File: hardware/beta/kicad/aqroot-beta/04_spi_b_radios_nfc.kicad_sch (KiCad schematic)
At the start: 11 parts, among them U7 E07-400M10S, U8 E22-900M22S, U9 ST25R3916_NFC_PLACEHOLDER

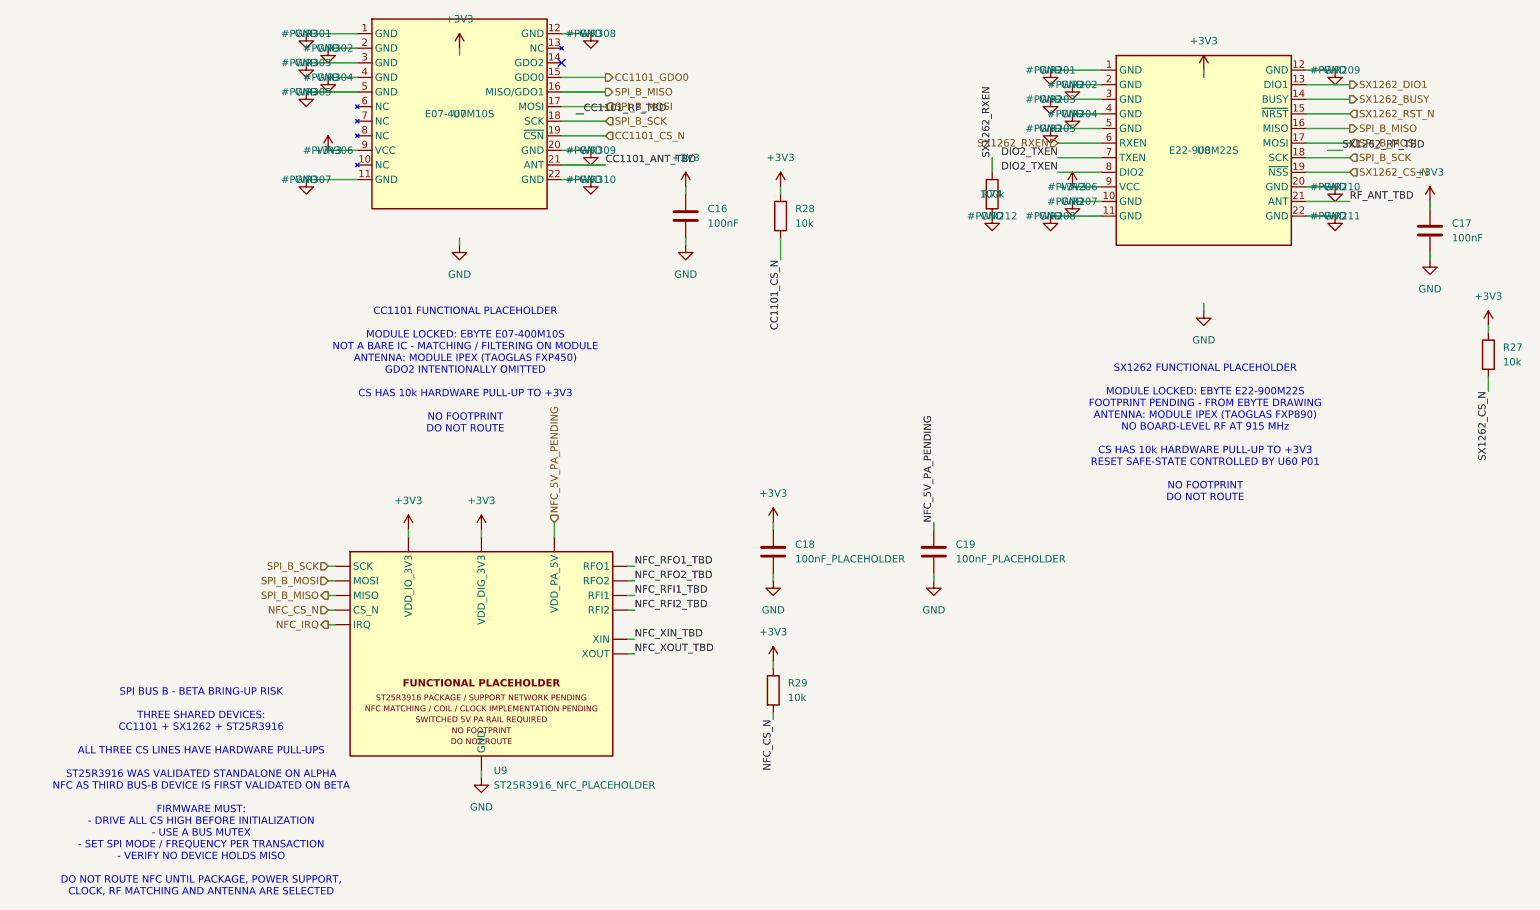
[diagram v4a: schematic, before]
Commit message: AQROOT Beta: integrate physical ST25R3916 NFC controller
Replaces the 15-pin ST25R3916_NFC_PLACEHOLDER at U9 with the physical 33-pad
ST25R3916-AQET on AQROOT_Beta:ST25R3916_AQET, and adds the ten ST-specified
decoupling capacitors. Single sheet touched, 04_spi_b_radios_nfc, plus two pin
electrical types corrected in the library.

ALL 33 PADS VERIFIED AGAINST AN EXPECTED MAP, not merely counted: the netlist was
compared pin-by-pin to the locked mapping and returned 33 of 33 with zero
mismatches. Supplies are VDD_IO on +3V3, VDD and VDD_TX both on
NFC_5V_PA_PENDING, and I2C_EN grounded to select SPI. SPI is BSS on pin 29 to
NFC_CS_N, SCLK/MOSI/MISO to SPI bus B, IRQ on pin 27 to NFC_IRQ. Grounds are
GND_D, both GND_DR, VSS, GND_A and the exposed pad 33.

THE KEY RELATIONSHIP IS CORRECT IN THE NETLIST: NFC_VDD_RF holds U9 pin 9,
U9 pin 14, C49 and C50 - the VDD_RF regulator output feeding VDD_DR with its
decoupling, which is the normal internal-regulator configuration. There is no
VDD_DR to VDD_TX and no VDD_RF to VDD_TX connection anywhere; the bypass mode is
not implemented.

TEN CAPACITORS ADDED, C45 to C54, values exactly as ST specifies and not
substituted: VDD_D 2.2uF with 10nF, VDD_A 2.2uF with 10nF, VDD_RF 2.2uF with
10nF, VDD_AM 2.2uF with 1nF, and AGDC 1uF with 10nF. The 2.2uF parts are 16V X7R
in 0805 rather than 0603 so effective capacitance survives bias, the small values
are 50V X7R 0603, and the 1uF is 16V X7R 0603. Each carries a note that it is
local decoupling requiring close placement during layout.

TWO ERC ERRORS WERE FIXED BY CORRECTING THE MODEL RATHER THAN BY ADDING
EXCLUSIONS. VDD_RF was typed as a plain output, so the power input VDD_DR it
feeds reported power_pin_not_driven; VDD_RF is genuinely a regulated supply
output and is now typed power_out, which removes the error legitimately. RFI1,
RFI2 and XTI were typed as inputs and reported pin_not_driven on their deferred
analog nets; they are analog pins into networks that do not yet exist, an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
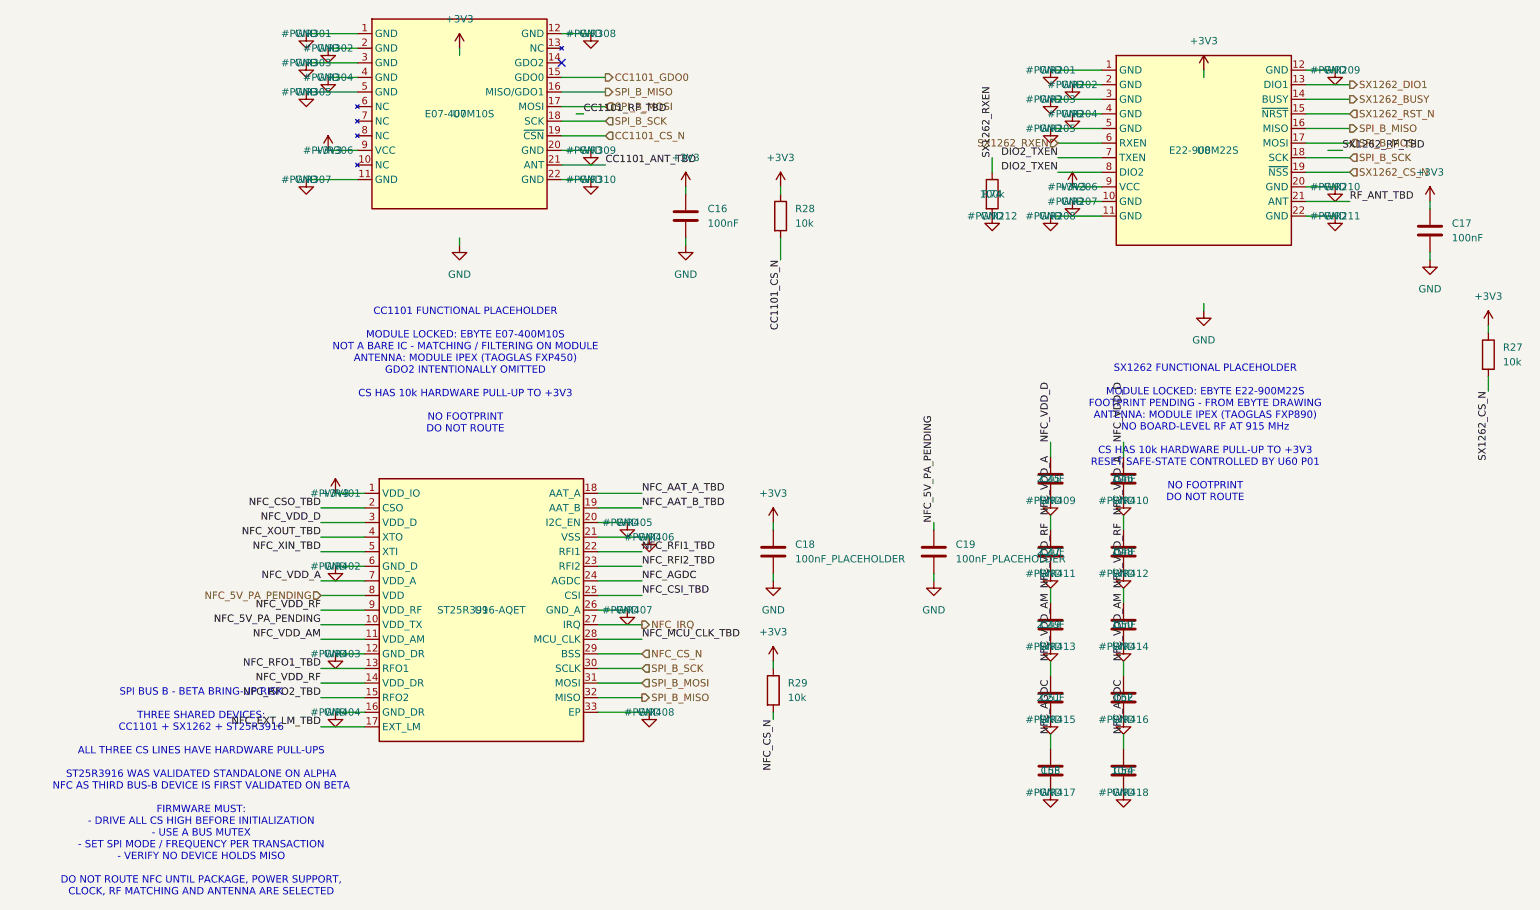
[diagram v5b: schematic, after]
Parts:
- removed U9: ST25R3916_NFC_PLACEHOLDER, symbol AQROOT_Beta:ST25R3916_NFC_PLACEHOLDER
- added C45, C47, C49, C51: 2.2uF, Capacitor_SMD:C_0805_2012Metric, symbol Device:C
- added C46, C48, C50, C54: 10nF, Capacitor_SMD:C_0603_1608Metric, symbol Device:C
- added C52: 1nF, Capacitor_SMD:C_0603_1608Metric, symbol Device:C
- added C53: 1uF, Capacitor_SMD:C_0603_1608Metric, symbol Device:C
- added U9: ST25R3916-AQET, AQROOT_Beta:ST25R3916_AQET, symbol AQROOT_Beta:ST25R3916-AQET
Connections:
- net +3V3: now also U9.1 (VDD_IO)
- net GND: now also C45.2, C46.2, C47.2, C48.2, C49.2, C50.2, C51.2, C52.2, C53.2, C54.2, U9.12 (GND_DR), U9.16 (GND_DR), U9.20 (I2C_EN), U9.21 (VSS), U9.26 (GND_A), U9.33 (EP), U9.6 (GND_D)
- net NFC_5V_PA_PENDING: now also U9.10 (VDD_TX), U9.8 (VDD)
- net NFC_CS_N: now also U9.29 (BSS)
- net NFC_IRQ: now also U9.27 (IRQ)
- net NFC_RFI1_TBD: now also U9.22 (RFI1)
- net NFC_RFI2_TBD: now also U9.23 (RFI2)
- net NFC_RFO1_TBD: now also U9.13 (RFO1)
- net NFC_RFO2_TBD: now also U9.15 (RFO2)
- net NFC_XIN_TBD: now also U9.5 (XTI)
- net NFC_XOUT_TBD: now also U9.4 (XTO)
- net SPI_B_MISO: now also U9.32 (MISO)
- net SPI_B_MOSI: now also U9.31 (MOSI)
- net SPI_B_SCK: now also U9.30 (SCLK)
- new net NFC_AAT_A_TBD: U9.18 (AAT_A)
- new net NFC_AAT_B_TBD: U9.19 (AAT_B)
- new net NFC_AGDC: C53.1, C54.1, U9.24 (AGDC)
- new net NFC_CSI_TBD: U9.25 (CSI)
- new net NFC_CSO_TBD: U9.2 (CSO)
- new net NFC_EXT_LM_TBD: U9.17 (EXT_LM)
- new net NFC_MCU_CLK_TBD: U9.28 (MCU_CLK)
- new net NFC_VDD_A: C47.1, C48.1, U9.7 (VDD_A)
- new net NFC_VDD_AM: C51.1, C52.1, U9.11 (VDD_AM)
- new net NFC_VDD_D: C45.1, C46.1, U9.3 (VDD_D)
- new net NFC_VDD_RF: C49.1, C50.1, U9.14 (VDD_DR), U9.9 (VDD_RF)

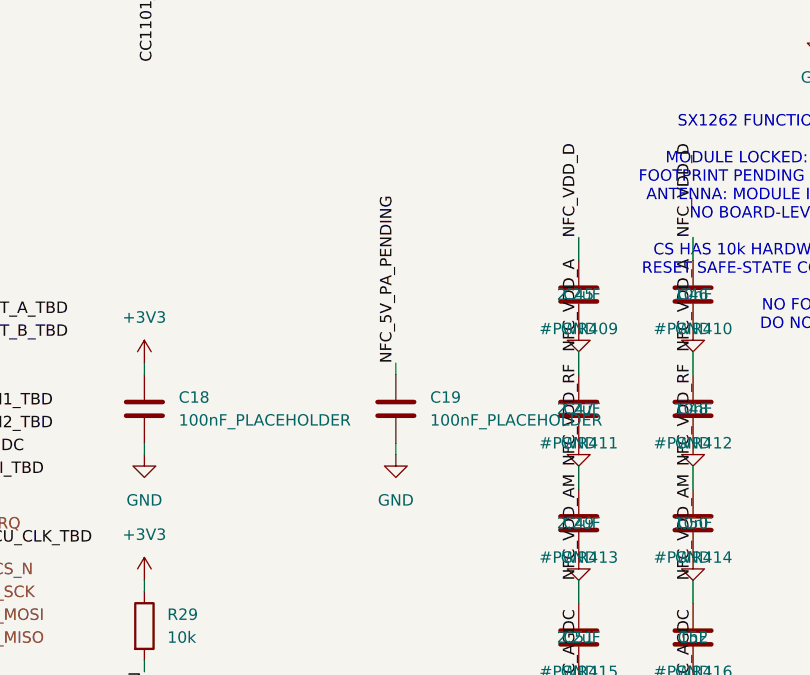
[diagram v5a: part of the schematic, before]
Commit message: AQROOT Beta: finalize NFC external decoupling
C18 = 100nF, 16 V, X7R, 0402. Role was already proven in the capture:
+3V3 -> C18 -> GND, ST25R3916 VDD_IO external supply decoupling. PLACEHOLDER
wording retired. VDD_D, VDD_A, VDD_RF, VDD_AM and AGDC decoupling are captured
separately and were not touched.

C19 = 100nF, 16 V, X7R, 0402. Role already proven: NFC_5V_PA_PENDING -> C19 ->
GND, external VDD / VDD_TX high-frequency decoupling. PLACEHOLDER wording
retired. C19 stays the HF decoupler and is explicitly NOT replaced by the bulk
capacitor.

C55 = 2.2uF, 16 V, X7R, 0805 - NEW component, authorised in the ratified lock.
NFC_5V_PA_PENDING -> C55 -> GND, placed electrically at the ST25R3916 external
VDD / VDD_TX supply input beside C19, providing local bulk decoupling for the
pulsed NFC transmitter current. C55 is the next free capacitor reference; no
existing reference was reused. Value is LOCKED FOR BETA but carries an explicit
note that it is TO BE RECONFIRMED DURING ST REFERENCE / BOM REVIEW.

All three are STANDARD_EIA_PASSIVE with BOM class and approved alternates rather
than premium single MPNs. DC-bias derating on C55 is flagged for BOM-lock
validation.

No NFC RF or matching TBD network was touched.

Netlist delta is exactly the intended one: C55 appears on /NFC_5V_PA_PENDING and
GND, no other component changes any pin's net, and the net count is unchanged at
174 because C55 joins two existing nets. Component count 186 -> 187. Canonical
ERC holds at 58 raw / 5 errors / 53 warnings with 58 live exclusions, 0 stale
and 0 unexplained real defects.

Co-Authored-By: Claude Opus 5 <noreply@anthropic.com>
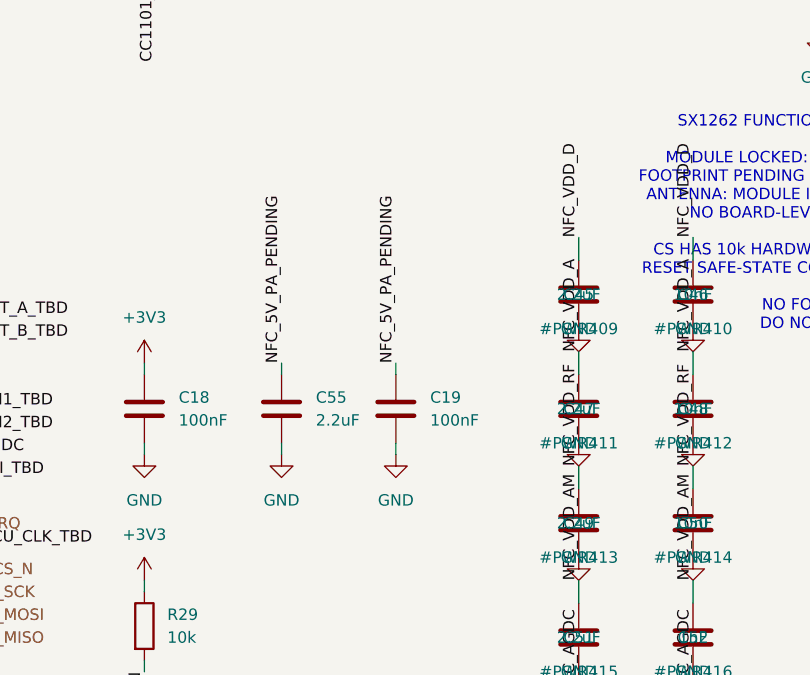
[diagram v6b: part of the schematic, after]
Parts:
- added C55: 2.2uF, Capacitor_SMD:C_0805_2012Metric, symbol Device:C
- C18: value 100nF_PLACEHOLDER -> 100nF; footprint (none) -> Capacitor_SMD:C_0402_1005Metric; BOM_Class (none) -> STANDARD_EIA_PASSIVE - multi-source, approved alternates, n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; Dielectric (none) -> X7R; Note (none) -> ST25R3916 VDD_IO external supply decoupling: +3V3 -> C18 ->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; Package (none) -> 0402 (1005 metric); Voltage (none) -> 16V
- C19: value 100nF_PLACEHOLDER -> 100nF; footprint (none) -> Capacitor_SMD:C_0402_1005Metric; BOM_Class (none) -> STANDARD_EIA_PASSIVE - multi-source, approved alternates, n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; Dielectric (none) -> X7R; Note (none) -> ST25R3916 external VDD / VDD_TX high-frequency decoupling: 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; Package (none) -> 0402 (1005 metric); Voltage (none) -> 16V
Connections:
- net GND: now also C55.2
- net NFC_5V_PA_PENDING: now also C55.1

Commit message: AQROOT Beta: correct NFC TX bulk decoupling
C55 is the one placement-lock exception the ruling authorised. It moves
from (10.000, 19.000) rot 0 to (22.225, 29.400) rot 270, with pad 1
(NFC_5V_PA_PENDING) facing north at U9 pins 8/10 and pad 2 (GND) south,
so the return loop closes away from U9's RF pins.

  C55 pad1 -> U9 pin 8  (VDD_TX): 14.005 mm -> 4.875 mm
  C55 pad1 -> U9 pin 10 (VDD_TX): 15.148 mm -> 4.469 mm

The <=3.0 mm electrical target is NOT met, and that is structural, not
an oversight. An exhaustive search over every 0.05 mm position, four
rotations and both 0603/0805 classes, rejected against every locked
F.Cu courtyard, found 680,610 legal positions whose best worst-case
distance is 4.813 mm. C50 (10 nF) and C52 (1 nF) hold the only space
within 3 mm of U9's south edge; the gap between U9 and them is 1.13 mm,
narrower than any 0603 or 0805 courtyard, and neither is authorised to
move. C19 (100 nF, same net) was already 4.309 mm away.

Footprint changed 0805 -> 0603 under the ruling's authorisation, with
the schematic Footprint/Package fields updated to match. The reason is
not the 0.087 mm distance gain: no 2.2 uF >=10 V X7R MLCC in either
package has a documented MAX height <=0.80 mm. Murata GRM21BR71E225KA73
(0805, 25 V) is 1.25 +/-0.15 -> 1.40 mm max; 0603 at this value is
0.80 +/-0.10 -> 0.90 mm max. 0603 turns a 0.60 mm miss into a 0.10 mm
miss, and 0603/16 V X7R holds >=1.2 uF at 5 V with margin. Value is
unchanged and the MPN remains a BOM verification item.

The move places C55 inside the TOP panel shadow, so it now carries the
<=0.80 mm ceiling and joins the panel-height ledger. Every position
that improves on 14.005 mm is inside that shadow. Separately, U9 itself
already exceeds the ceiling - ST DS12484 Rev 3 Table 134 gives
VFQFPN32 A = 0.800/0.900/1.000 mm - which suggests the 0.80 mm figure
is a nominal being applied as a maximum.

C45/C47/C49/C51 were examined and deliberately left: their distance is
dominated by X, freeing C55's old sl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
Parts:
- C55: footprint Capacitor_SMD:C_0805_2012Metric -> Capacitor_SMD:C_0603_1608Metric; Note ST25R3916 VDD / VDD_TX local BULK decoupling for pulsed NFC transmitter current: NFC_5V_PA_PENDING -> C55 -> GND, placed electrically at the external supply input alongside the C19 HF decoupler. LOCKED VALUE FOR BETA, but VALUE TO BE RECONFIRMED DURING ST REFERENCE / BOM REVIEW. -> ST25R3916 VDD / VDD_TX local BULK decoupling for pulsed NFC transmitter current: NFC_5V_PA_PENDING -> C55 -> GND, placed electrically at the external supply input alongside the C19 HF decoupler. LOCKED VALUE FOR BETA, but VALUE TO BE RECONFIRMED DURING ST REFERENCE / BOM REVIEW. 2026-08-11 pre-routing pass: package changed 0805 -> 0603 and the part moved from (10.0, 19.0) to (22.225, 29.40) rot 270, giving 4.875 mm to U9 pin 8 and 4.469 mm to pin 10 (CTO target was <=3.0 mm; NOT met - C50 and C52 hold the only closer space and placement is locked). The new position is inside the TOP panel shadow X12-62 Y9-78, so C55 now carries the <=0.80 mm panel ceiling. NO 2.2uF >=10V X7R MLCC in 0603 or 0805 has a documented MAX height <=0.80 mm (0603 is 0.80+/-0.10 -> 0.90 max; Murata GRM21BR71E225KA73 0805 is 1.25+/-0.15 -> 1.40 max), so height is an OPEN BOM/MECH item shared with the other 0603s already in the panel shadow. DC-bias requirement: >=1.2 uF effective at 5.0 V - 16 V X7R 0603 is spe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; Package 0805 (2012 metric) -> 0603 (1608 metric)
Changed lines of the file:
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@@
 			)
 		)
-		(property "Footprint" "Capacitor_SMD:C_0805_2012Metric"
+		(property "Footprint" "Capacitor_SMD:C_0603_1608Metric"
 			(at 158.445 137.16 0)
 			(hide yes)
@@
 			)
 		)
-		(property "Package" "0805 (2012 metric)"
+		(property "Package" "0603 (1608 metric)"
 			(at 157.48 133.35 0)
 			(hide yes)
@@
 			)
 		)
-		(property "Note" "ST25R3916 VDD / VDD_TX local BULK decoupling for pulsed NFC transmitter current: NFC_5V_PA_PENDING -> C55 -> GND, placed electrically at the external supply input alongside the C19 HF decoupler. LOCKED VALUE FOR BETA, but VALUE TO BE RECONFIRMED DURING ST REFERENCE / BOM REVIEW."
+		(property "Note" "ST25R3916 VDD / VDD_TX local BULK decoupling for pulsed NFC transmitter current: NFC_5V_PA_PENDING -> C55 -> GND, placed electrically at the external supply input alongside the C19 HF decoupler. LOCKED VALUE FOR BETA, but VALUE TO BE RECONFIRMED DURING ST REFERENCE / BOM REVIEW. 2026-08-11 pre-routing pass: package changed 0805 -> 0603 and the part moved from (10.0, 19.0) to (22.225, 29.40) rot 270, giving 4.875 mm to U9 pin 8 and 4.469 mm to pin 10 (CTO target was <=3.0 mm; NOT met - C50 and C52 hold the only closer space and placement is locked). The new position is inside the TOP panel shadow X12-62 Y9-78, so C55 now carries the <=0.80 mm panel ceiling. NO 2.2uF >=10V X7R MLCC in 0603 or 0805 has a documented MAX height <=0.80 mm (0603 is 0.80+/-0.10 -> 0.90 max; Murata GRM21BR71E225KA73 0805 is 1.25+/-0.15 -> 1.40 max), so height is an OPEN BOM/MECH item shared with the other 0603s already in the panel shadow. DC-bias requirement: >=1.2 uF effective at 5.0 V - 16 V X7R 0603 is specified for that margin."
 			(at 157.48 133.35 0)
 			(hide yes)
